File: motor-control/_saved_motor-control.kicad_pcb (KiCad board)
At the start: 2 copper layers, 74 parts, among them P1 CONN_02X12, P2 to_motor_phase_1, P3 to_motor_phase_2, P4 to_motor_phase_3, P5 CONN_01X01, P6 CONN_01X01, Q1 CSD19536KTT, Q10 CSD19536KTT, Q11 CSD19536KTT, Q12 CSD19536KTT, Q2 CSD19536KTT, Q3 CSD19536KTT, Q4 CSD19536KTT, Q5 CSD19536KTT, Q6 CSD19536KTT, Q7 CSD19536KTT, Q8 CSD19536KTT, Q9 CSD19536KTT, U1 ACS770, U2 ACS770, U3 ACS770, U4 DRV8301

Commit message: more layout changes
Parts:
- C1, C16, C18, C2, C20, C4, C5, C6, Q1, Q10, Q11, Q12, Q2, Q3, Q4, Q5, Q6, Q7, Q8, Q9, R12, R13, R16, R19, R20, R21, R5, R6, R9, U1, U2, U3: moved to B.Cu
- moved C16 235.4 mm to (20.3, 16.5), turned to 270 degrees
- moved C11 226.7 mm to (67.3, 40.6)
- moved C8 224.6 mm to (63.5, 29.2), turned to 270 degrees
- moved C10 224.1 mm to (67.3, 38.1)
- moved C7 222.6 mm to (61.0, 29.2), turned to 270 degrees
- moved C9 221.6 mm to (67.3, 35.6), turned to 180 degrees
- moved R26 204.9 mm to (69.8, 27.9), turned to 270 degrees
- moved D1 204.6 mm to (100.3, 33.7), turned to 270 degrees
- moved C13 202.2 mm to (88.9, 22.9)
- moved R24 200.7 mm to (62.2, 33.0), turned to 180 degrees
- moved R25 199.6 mm to (72.4, 27.9), turned to 270 degrees
- moved C12 199.4 mm to (74.9, 34.3), turned to 270 degrees
- moved C19 196.1 mm to (117.1, 25.4)
- moved R14 195.9 mm to (101.0, 19.7)
- moved C17 194.1 mm to (111.8, 25.4)
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
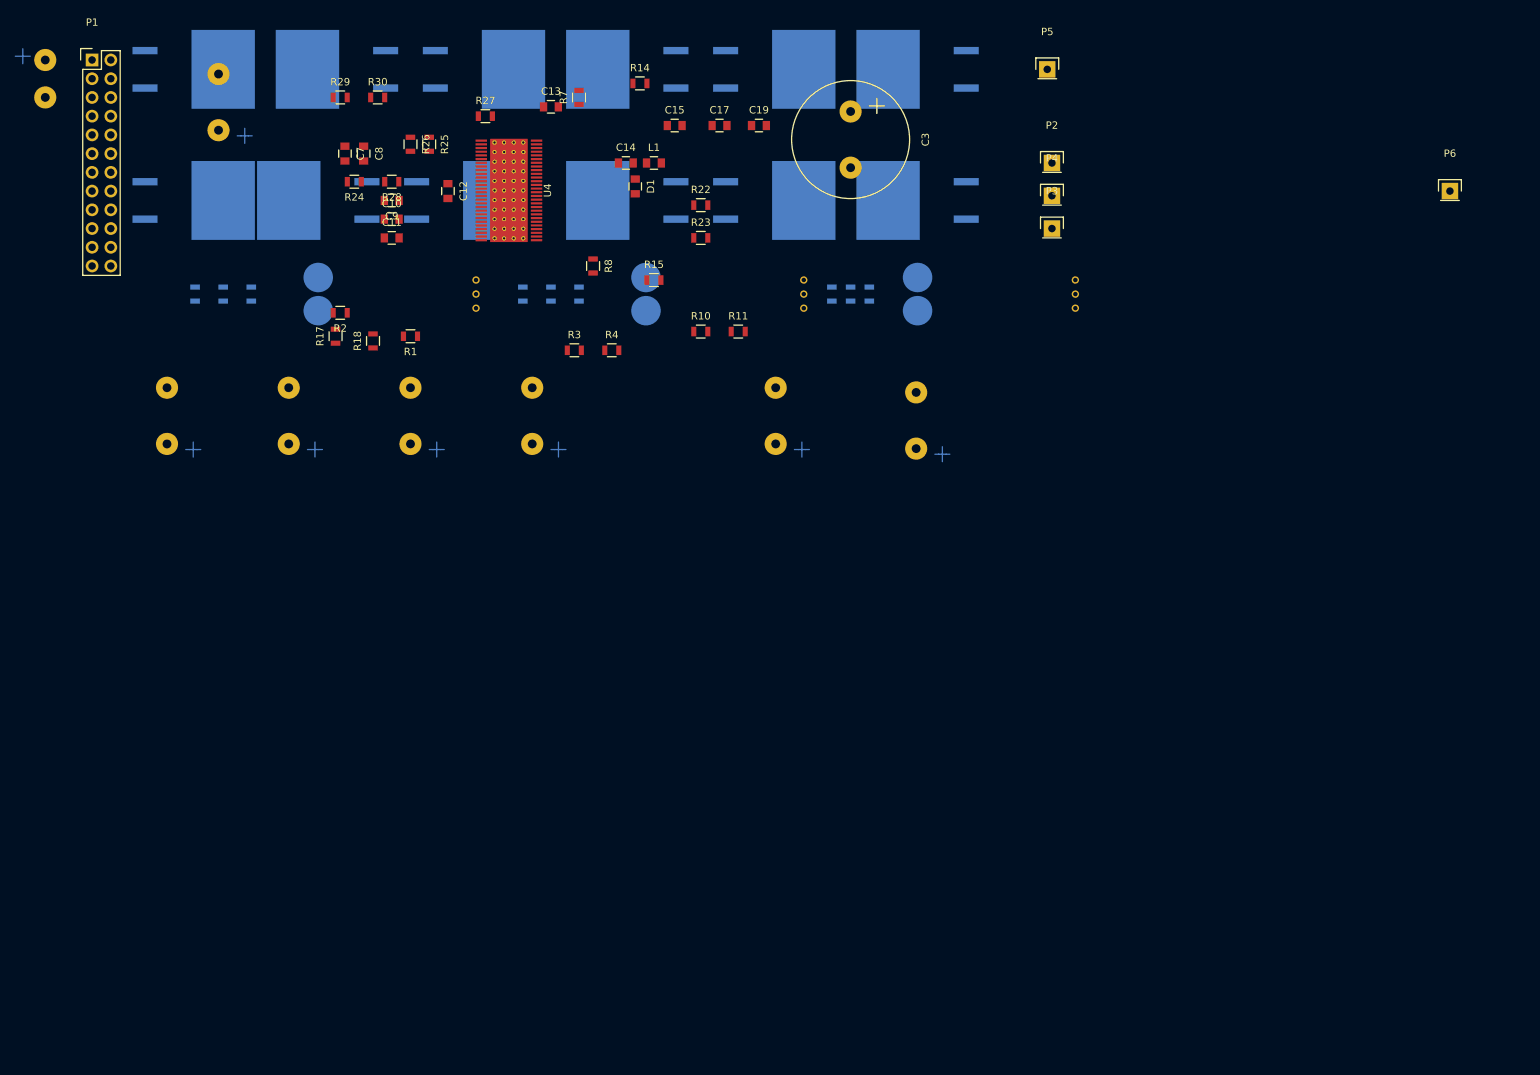
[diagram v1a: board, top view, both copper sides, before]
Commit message: Significant board changes, fixed hall ftpnt
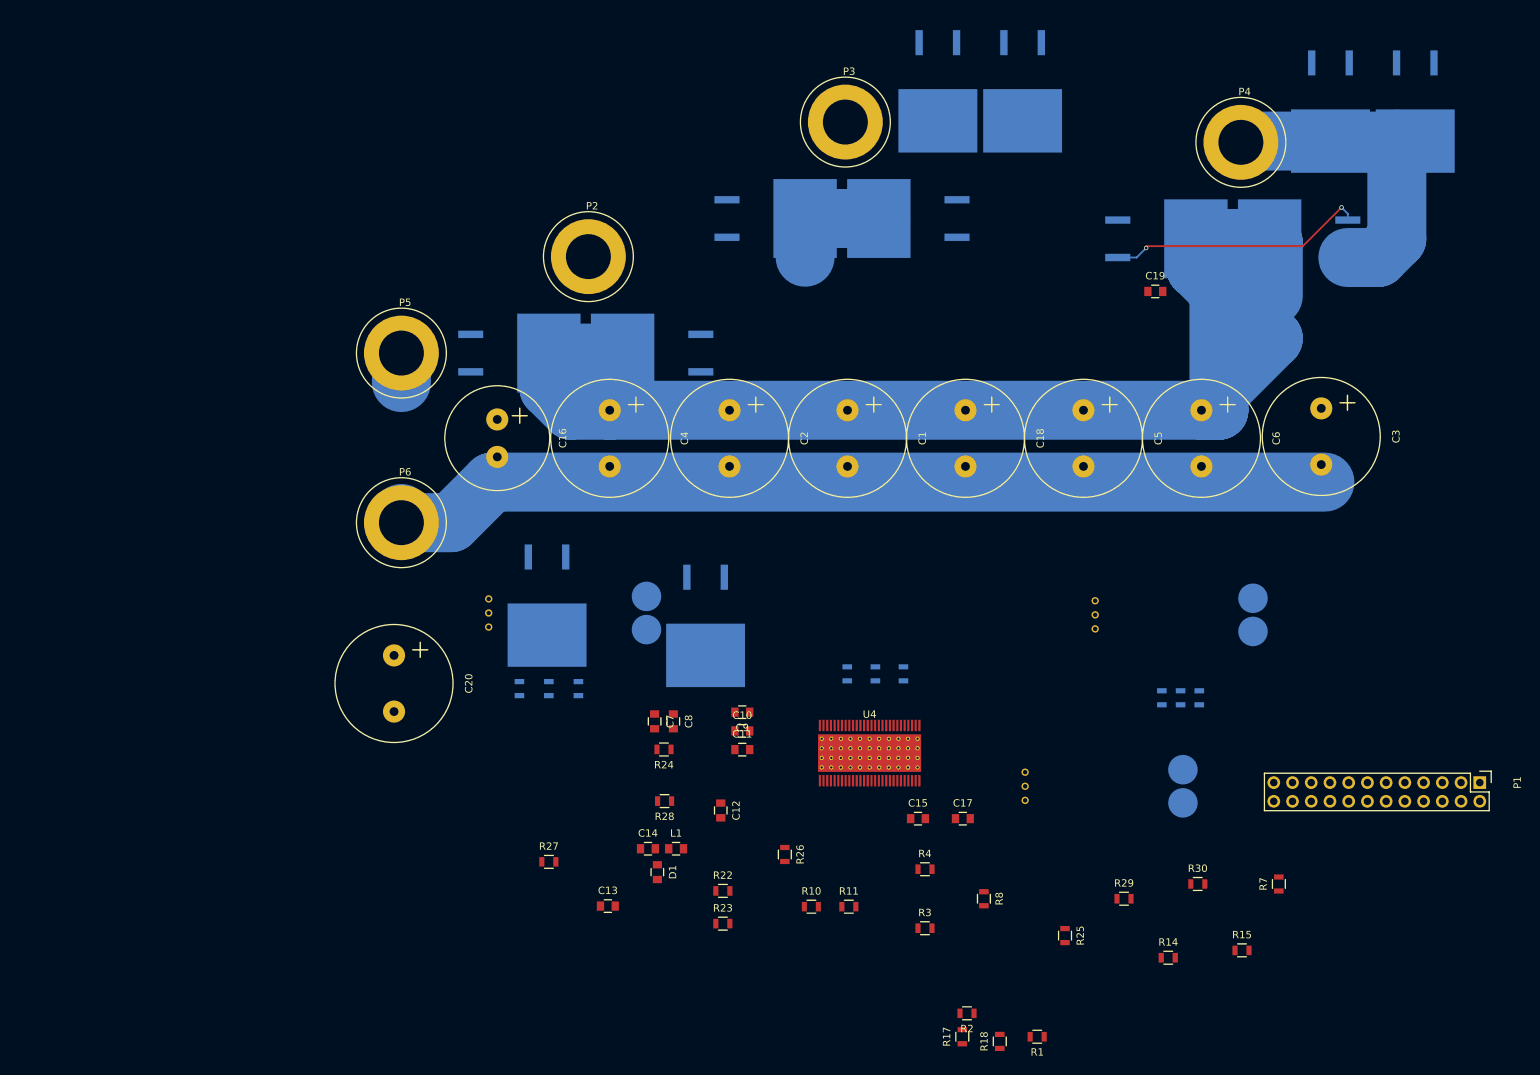
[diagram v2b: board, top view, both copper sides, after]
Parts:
- C1, C16, C18, C2, C20, C4, C5, C6: moved to F.Cu
- P2, P3, P4, P5, P6: footprint Pin_Headers:Pin_Header_Straight_1x01 -> Connect:Banana_Jack_1Pin
- moved P1 212.2 mm to (214.9, 114.5), turned to 270 degrees
- moved R30 154.1 mm to (176.6, 128.3)
- moved R29 152.0 mm to (166.6, 130.3)
- moved P6 149.1 mm to (68.6, 79.3)
- moved R7 142.8 mm to (187.6, 128.3)
- moved R14 138.5 mm to (172.6, 138.3)
- moved R25 137.7 mm to (158.6, 135.3)
- moved R18 127.5 mm to (149.8, 149.6)
- moved R1 127.5 mm to (154.8, 149.0)
- moved R17 127.5 mm to (144.7, 149.0)
- moved R2 127.5 mm to (145.3, 145.8)
- moved R15 120.9 mm to (182.6, 137.3)
- moved U2 115.9 mm to (163.4, 115.0), turned to 90 degrees
- moved R26 108.9 mm to (120.6, 124.3)
- moved C13 108.7 mm to (96.6, 131.3)
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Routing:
- net +batt: track 0.00 -> 228.1 mm
- net GND: track 0.00 -> 128.8 mm
- net /Gate-Driver/SH_C: track 0.00 -> 42.5 mm
- net Net-(Q11-Pad1): track 0.00 -> 35.4 mm, vias 0 -> 2

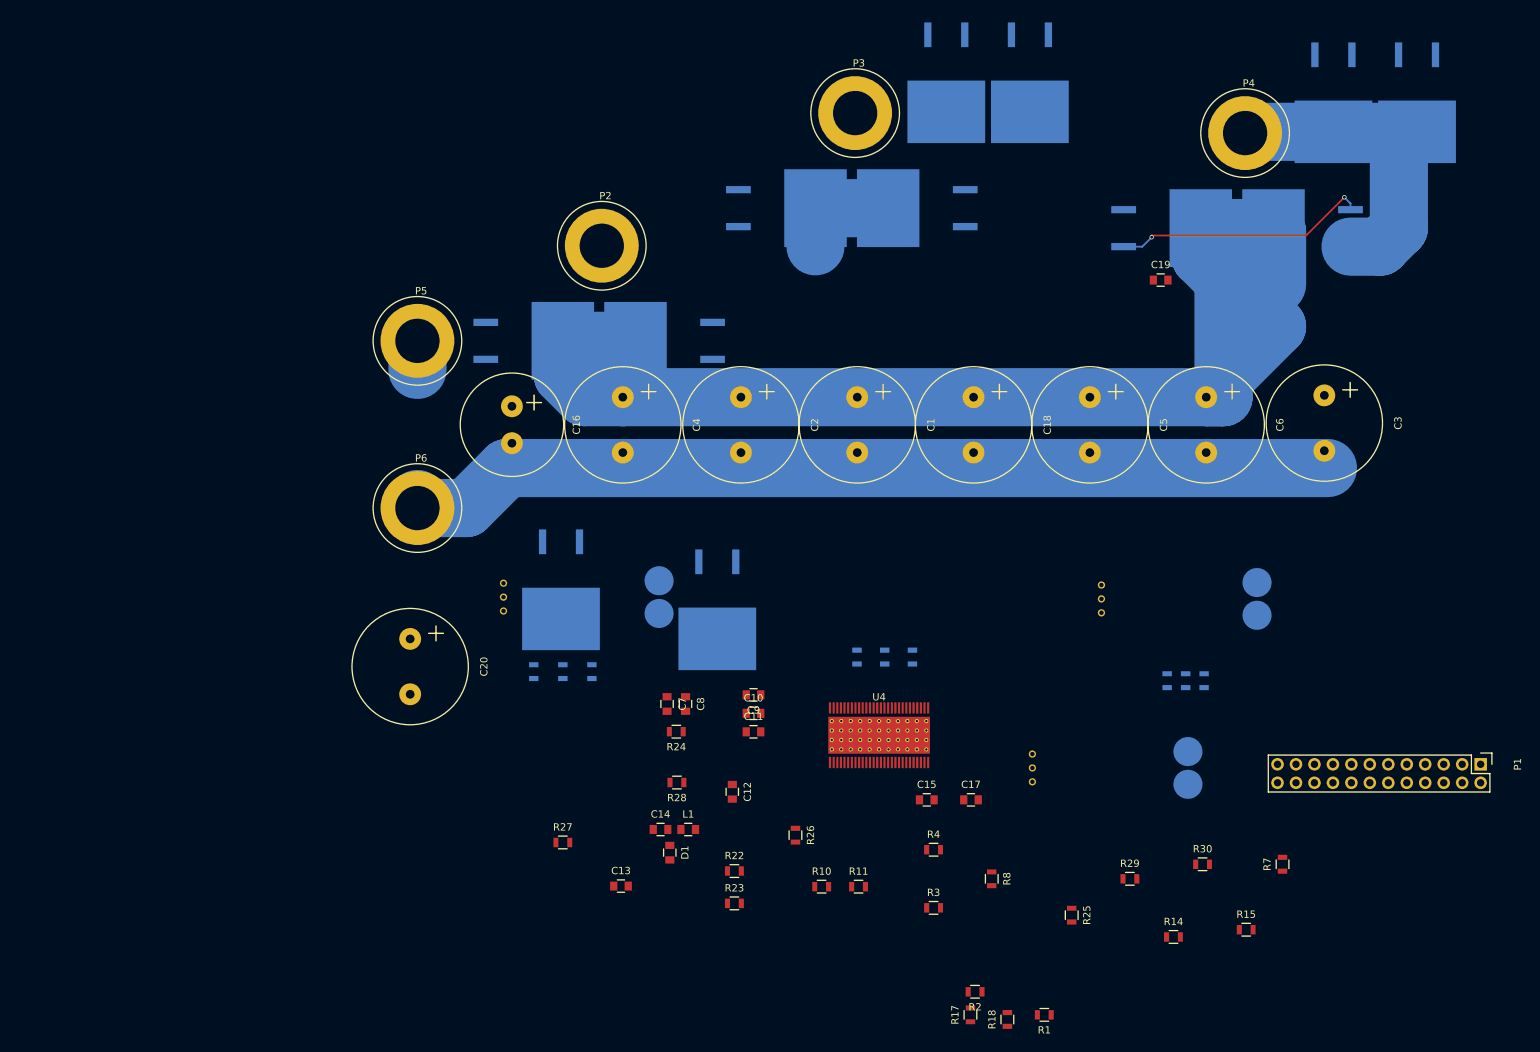
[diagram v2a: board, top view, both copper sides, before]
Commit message: Made prel design for back, started traces on front
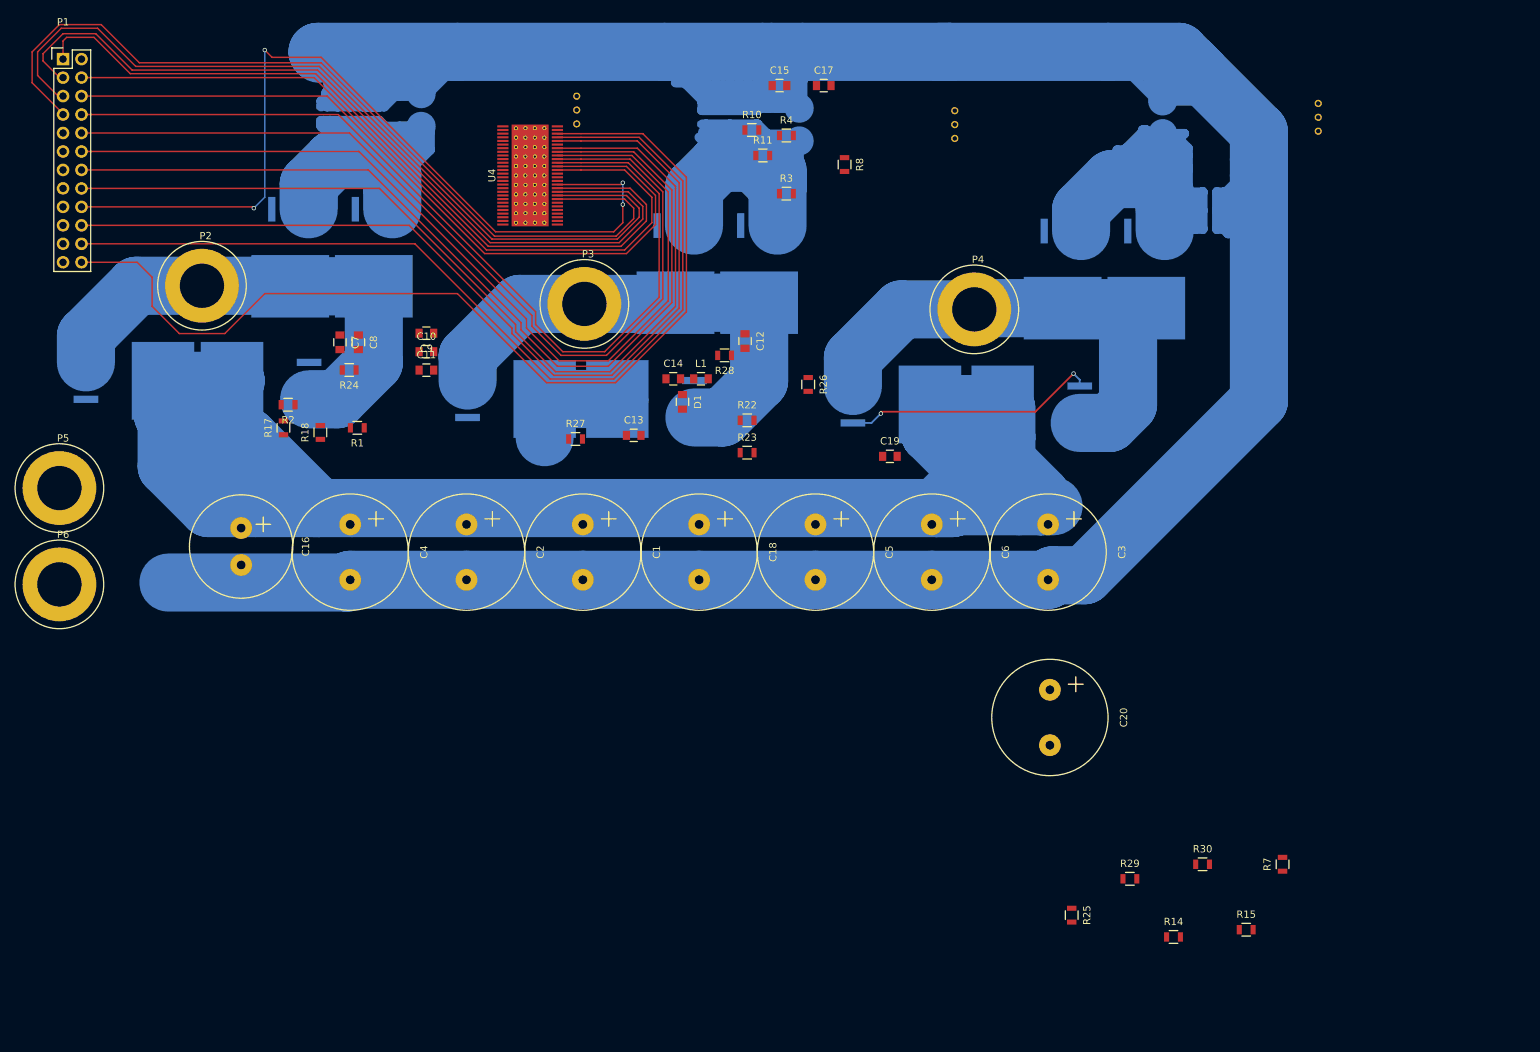
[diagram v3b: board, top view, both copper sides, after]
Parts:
- moved P1 217.8 mm to (19.9, 17.5), turned to 0 degrees
- moved R18 124.3 mm to (55.3, 68.9)
- moved R1 124.3 mm to (60.4, 68.2)
- moved R17 124.3 mm to (50.2, 68.2)
- moved R2 124.3 mm to (50.8, 65.0)
- moved R10 104.5 mm to (114.6, 27.3)
- moved R11 101.4 mm to (116.1, 30.8)
- moved C15 100.3 mm to (118.4, 21.1)
- moved R3 100.3 mm to (119.4, 36.0)
- moved R4 100.3 mm to (119.4, 28.0)
- moved R8 100.3 mm to (127.4, 32.0)
- moved C17 100.3 mm to (124.5, 21.1)
- moved U2 93.8 mm to (132.4, 26.5), turned to 270 degrees
- moved U4 90.7 mm to (84.1, 33.5), turned to 90 degrees
- moved C20 88.3 mm to (155.6, 104.3)
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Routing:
- net GND: track 128.8 -> 656.1 mm
- net /Gate-Driver/SL_A: track 0.00 -> 149.8 mm
- net /Gate-Driver/S02: track 0.00 -> 139.7 mm
- net /Gate-Driver/SL_B: track 0.00 -> 133.0 mm
- net /Gate-Driver/SL_C: track 0.00 -> 132.8 mm
- net /Gate-Driver/S01: track 0.00 -> 131.8 mm
- net /Gate-Driver/REF: track 0.00 -> 131.4 mm
- net /Gate-Driver/INL_C: track 0.00 -> 131.4 mm
- net /Gate-Driver/INH_C: track 0.00 -> 130.0 mm
- net /Gate-Driver/INL_B: track 0.00 -> 129.1 mm
- net /Gate-Driver/INH_B: track 0.00 -> 127.8 mm
- net /Gate-Driver/INL_A: track 0.00 -> 127.1 mm
- net /Gate-Driver/DC_CAL: track 0.00 -> 120.9 mm, vias 0 -> 4
- net /Gate-Driver/nSCS: track 0.00 -> 120.2 mm
- net /Gate-Driver/SDI: track 0.00 -> 118.5 mm
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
